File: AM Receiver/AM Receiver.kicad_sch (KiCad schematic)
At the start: 5 parts

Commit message: Finished PCB design for AM Receiver and fixed all remaining errors
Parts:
- H100: renamed from H1; now fitted
- H101: renamed from H3; now fitted
- H102: renamed from H2; now fitted
- H103: renamed from H4; now fitted
- PCB100: renamed from PCB1; now fitted
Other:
- note added: "Changes, Modifications V1.0 Initial Revision Input Voltage +/- 12V ... 15V"
- note added: "Date 01.07.2026"
- note added: "Name T.Brown"
- note added: "Rev. 1.0"
- note added: "Revision History"
- title: AM-Receiver -> AM Receiver

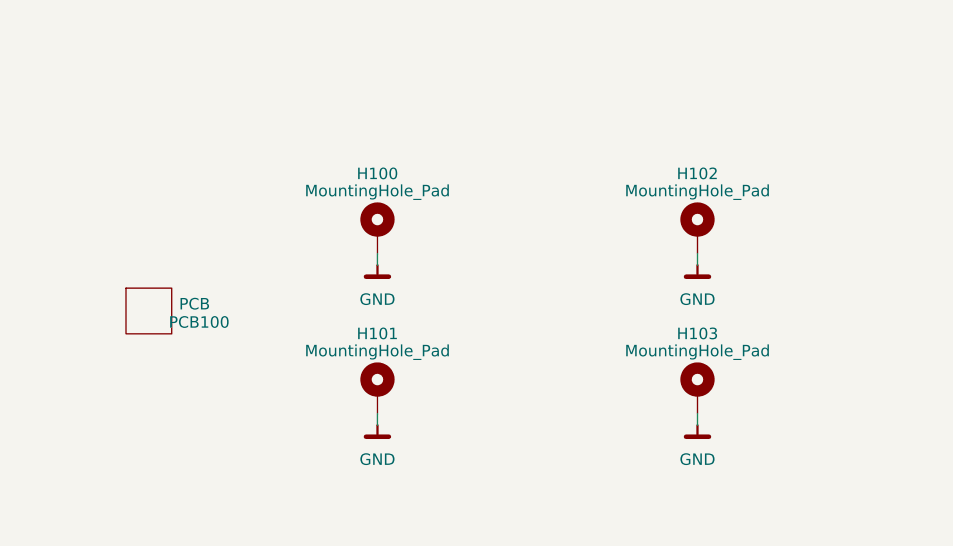
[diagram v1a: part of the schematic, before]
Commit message: Updated values of all resistors and capacitors
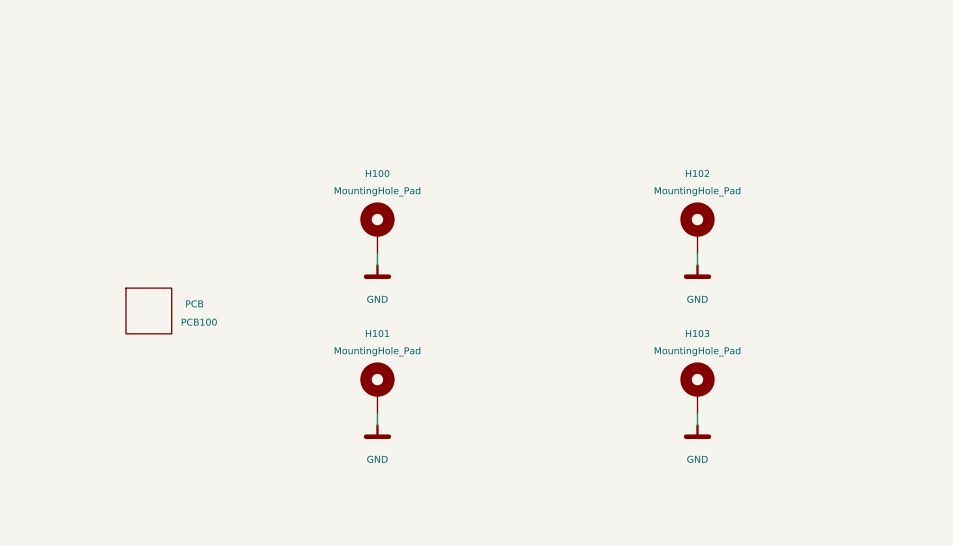
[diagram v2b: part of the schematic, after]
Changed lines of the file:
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@@
 			(effects
 				(font
-					(size 1.27 1.27)
+					(size 0.762 0.762)
 				)
 			)
@@
 			(effects
 				(font
-					(size 1.27 1.27)
+					(size 0.762 0.762)
 				)
 			)
@@
 			(effects
 				(font
-					(size 1.27 1.27)
+					(size 0.762 0.762)
 				)
 			)
@@
 			(effects
 				(font
-					(size 1.27 1.27)
+					(size 0.762 0.762)
 				)
 			)
@@
 			(effects
 				(font
-					(size 1.27 1.27)
+					(size 0.762 0.762)
 				)
 			)
@@
 			(effects
 				(font
-					(size 1.27 1.27)
+					(size 0.762 0.762)
 				)
 			)
@@
 			(effects
 				(font
-					(size 1.27 1.27)
+					(size 0.762 0.762)
 				)
 			)
@@
 			(effects
 				(font
-					(size 1.27 1.27)
+					(size 0.762 0.762)
 				)
 			)
@@
 			(effects
 				(font
-					(size 1.27 1.27)
+					(size 0.762 0.762)
 				)
 			)
@@
 			(effects
 				(font
-					(size 1.27 1.27)
+					(size 0.762 0.762)
 				)
 			)
@@
 			(effects
 				(font
-					(size 1.27 1.27)
+					(size 0.762 0.762)
 				)
 			)
@@
 			(effects
 				(font
-					(size 1.27 1.27)
+					(size 0.762 0.762)
 				)
 			)
@@
 			(effects
 				(font
-					(size 1.27 1.27)
+					(size 0.762 0.762)
 				)
 			)
@@
 			(effects
 				(font
-					(size 1.27 1.27)
+					(size 0.762 0.762)
 				)
 			)
@@
 			(effects
 				(font
-					(size 1.27 1.27)
+					(size 0.762 0.762)
 				)
 			)
@@
 			(effects
 				(font
-					(size 1.27 1.27)
+					(size 0.762 0.762)
 				)
 			)
@@
 			(effects
 				(font
-					(size 1.27 1.27)
+					(size 0.762 0.762)
 				)
 			)
@@
 			(effects
 				(font
-					(size 1.27 1.27)
-				)
-			)
+					(size 0.762 0.762)
+				)
+			)

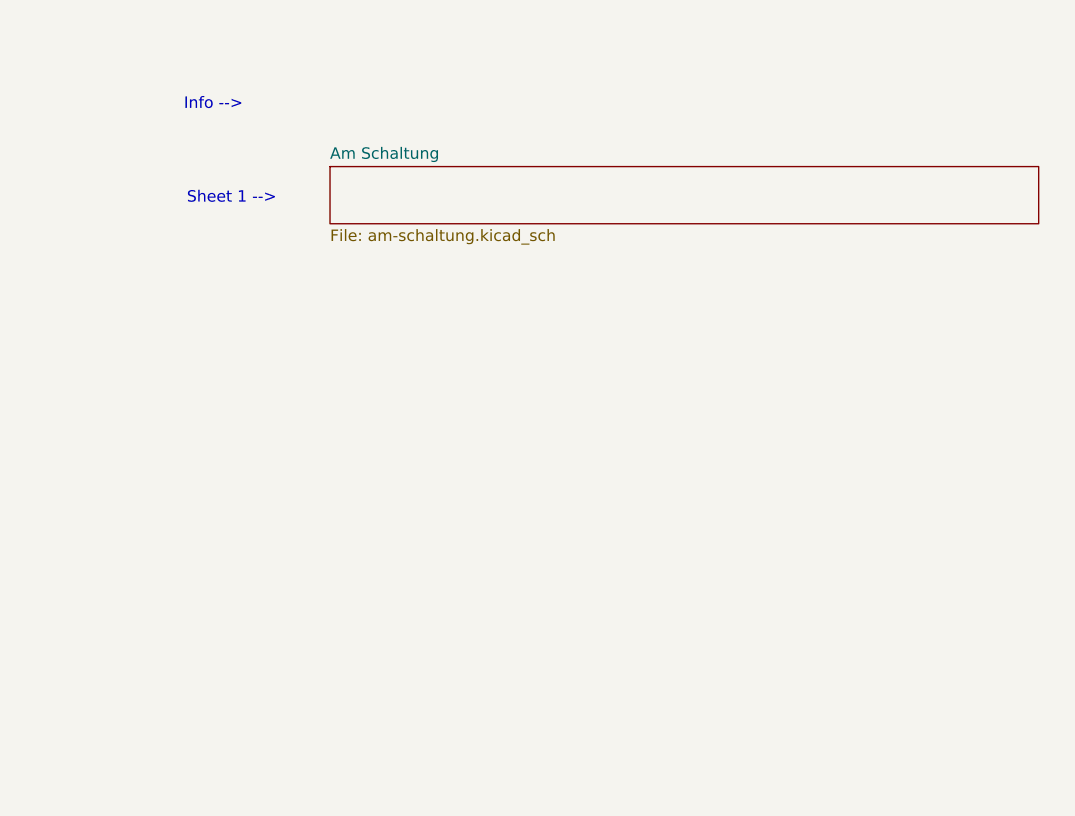
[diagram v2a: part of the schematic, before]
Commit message: Updated Schematic to use multiple sheets and repaired PCB
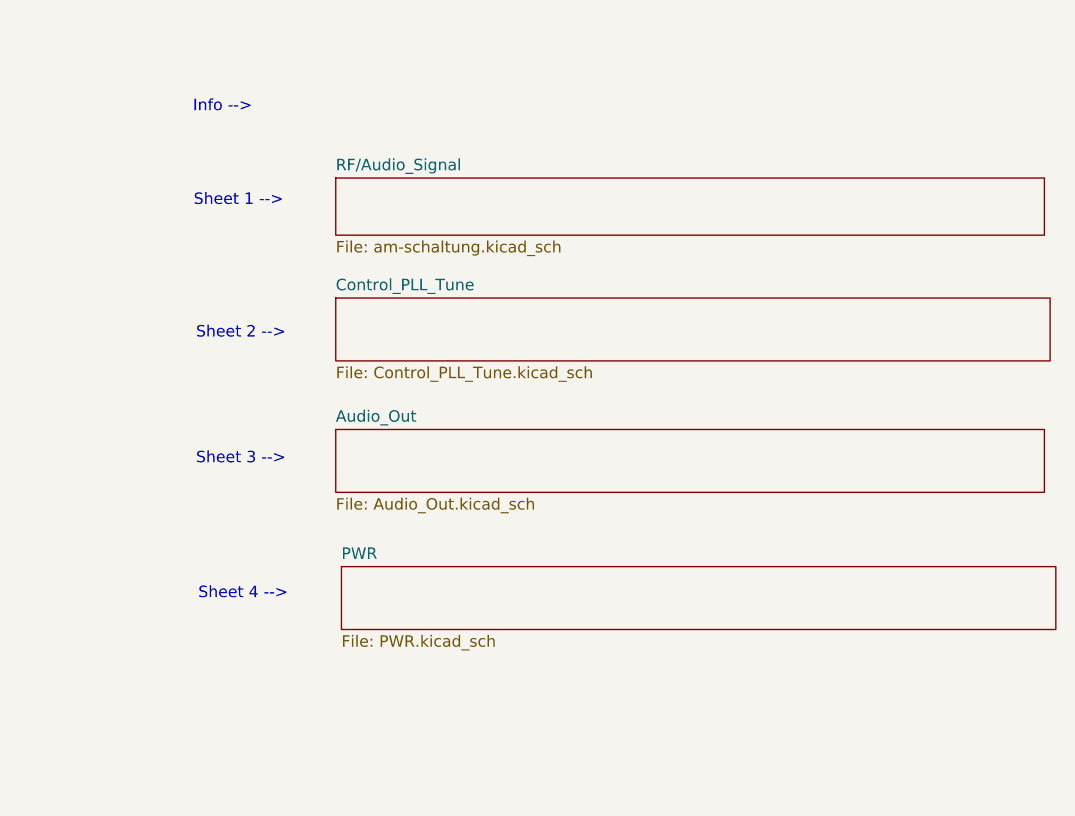
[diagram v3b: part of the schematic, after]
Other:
- sheet Am Schaltung renamed RF/Audio_Signal
- added sheet Audio_Out (Audio_Out.kicad_sch)
- added sheet Control_PLL_Tune (Control_PLL_Tune.kicad_sch)
- added sheet PWR (PWR.kicad_sch)
- note added: "Sheet 2 -->"
- note added: "Sheet 3 -->"
- note added: "Sheet 4 -->"
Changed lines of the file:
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@@
 	(title_block
 		(title "AM Receiver")
-		(date "2026-04-21")
+		(date "2026-07-06")
 		(rev "V1")
 		(company "HAWK")
@@
 	(text "Sheet 1 -->"
 		(exclude_from_sim no)
-		(at 189.738 35.306 0)
+		(at 190.5 35.56 0)
 		(effects
 			(font
@@
 	(text "Info -->"
 		(exclude_from_sim no)
-		(at 187.706 24.892 0)
+		(at 188.722 25.146 0)
+		(effects
+			(font
+				(size 1.27 1.27)
+			)
+		)
+	)
+	(text "Sheet 4 -->"
+		(exclude_from_sim no)
+		(at 191.008 79.248 0)
 		(effects
 			(font
@@
 		)
 	)
+	(text "Sheet 3 -->"
+		(exclude_from_sim no)
+		(at 190.754 64.262 0)
+		(effects
+			(font
+				(size 1.27 1.27)
+			)
+		)
+	)
 	(text "Name\nT.Brown"
 		(exclude_from_sim no)
@@
 			)
 			(justify left)
+		)
+	)
+	(text "Sheet 2 -->"
+		(exclude_from_sim no)
+		(at 190.754 50.292 0)
+		(effects
+			(font
+				(size 1.27 1.27)
+			)
 		)
 	)
@@
 	)
 	(sheet
-		(at 200.66 31.75)
-		(size 78.74 6.35)
+		(at 201.295 46.355)
+		(size 79.375 6.985)
 		(exclude_from_sim no)
 		(in_bom yes)
@@
 			(color 0 0 0 0)
 		)
-		(property "Sheetname" "Am Schaltung"
-			(at 200.66 31.0384 0)
+		(property "Sheetname" "Control_PLL_Tune"
+			(at 201.295 45.6434 0)
 			(show_name no)
 			(do_not_autoplace no)
@@
 			)
 		)
+		(property "Sheetfile" "Control_PLL_Tune.kicad_sch"
+			(at 201.295 53.9246 0)
+			(show_name no)
+			(do_not_autoplace no)
+			(effects
+				(font
+					(size 1.27 1.27)
+				)
+				(justify left top)
+			)
+		)
+		(instances
+			(project "AM Receiver"
+				(path "/fe1abb03-87b4-4c2c-a88f-7b58f4fb0195"
+					(page "3")
+				)
+			)
+		)
+	)
+	(sheet
+		(at 201.93 76.2)
+		(size 79.375 6.985)
+		(exclude_from_sim no)
+		(in_bom yes)
+		(on_board yes)
+		(dnp no)
+		(fields_autoplaced yes)
+		(stroke
+			(width 0.1524)
+			(type solid)
+		)
+		(fill
+			(color 0 0 0 0)
+		)
+		(property "Sheetname" "PWR"
+			(at 201.93 75.4884 0)
+			(show_name no)
+			(do_not_autoplace no)
+			(effects
+				(font
+					(size 1.27 1.27)
+				)
+				(justify left bottom)
+			)
+		)
+		(property "Sheetfile" "PWR.kicad_sch"
+			(at 201.93 83.7696 0)
+			(show_name no)
+			(do_not_autoplace no)
+			(effects
+				(font
+					(size 1.27 1.27)
+				)
+				(justify left top)
+			)
+		)
+		(instances
+			(project "AM Receiver"
+				(path "/fe1abb03-87b4-4c2c-a88f-7b58f4fb0195"
+					(page "5")
+				)
+			)
+		)
+	)
+	(sheet
+		(at 201.295 33.02)
+		(size 78.74 6.35)
+		(exclude_from_sim no)
+		(in_bom yes)
+		(on_board yes)
+		(dnp no)
+		(fields_autoplaced yes)
+		(stroke
+			(width 0.1524)
+			(type solid)
+		)
+		(fill
+			(color 0 0 0 0)
+		)
+		(property "Sheetname" "RF/Audio_Signal"
+			(at 201.295 32.3084 0)
+			(show_name no)
+			(do_not_autoplace no)
+			(effects
+				(font
+					(size 1.27 1.27)
+				)
+				(justify left bottom)
+			)
+		)
 		(property "Sheetfile" "am-schaltung.kicad_sch"
-			(at 200.66 38.6846 0)
+			(at 201.295 39.9546 0)
 			(show_name no)
 			(do_not_autoplace no)
@@
 				)
 			)
+		)
+	)
+	(sheet
+		(at 201.295 60.96)
+		(size 78.74 6.985)
+		(exclude_from_sim no)
+		(in_bom yes)
+		(on_board yes)
+		(dnp no)
+		(fields_autoplaced yes)
+		(stroke
+			(width 0.1524)
+			(type solid)
+		)
+		(fill
+			(color 0 0 0 0)
+		)
+		(property "Sheetname" "Audio_Out"
+			(at 201.295 60.2484 0)
+			(show_name no)
+			(do_not_autoplace no)
+			(effects
+				(font
+					(size 1.27 1.27)
+				)
+				(justify left bottom)
+			)
+		)
+		(property "Sheetfile" "Audio_Out.kicad_sch"
+			(at 201.295 68.5296 0)
+			(show_name no)
+			(do_not_autoplace no)
+			(effects
+				(font
+					(size 1.27 1.27)
+				)
+				(justify left top)
+			)
+		)
+		(instances
+			(project "AM Receiver"
+				(path "/fe1abb03-87b4-4c2c-a88f-7b58f4fb0195"
+					(page "4")
+				)
+			)

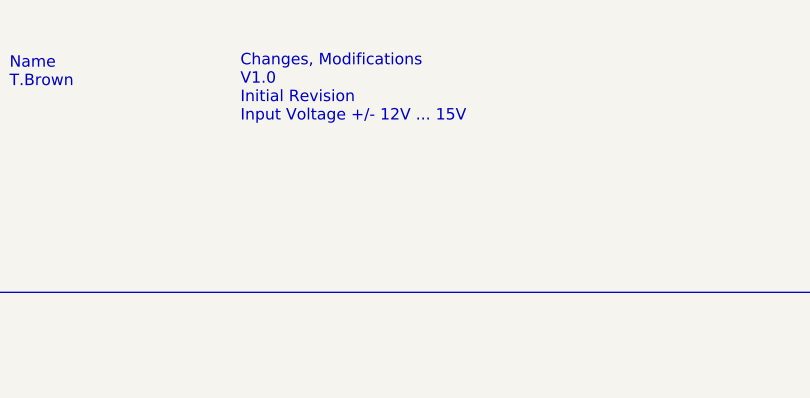
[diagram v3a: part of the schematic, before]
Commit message: updated schematic root page voltage
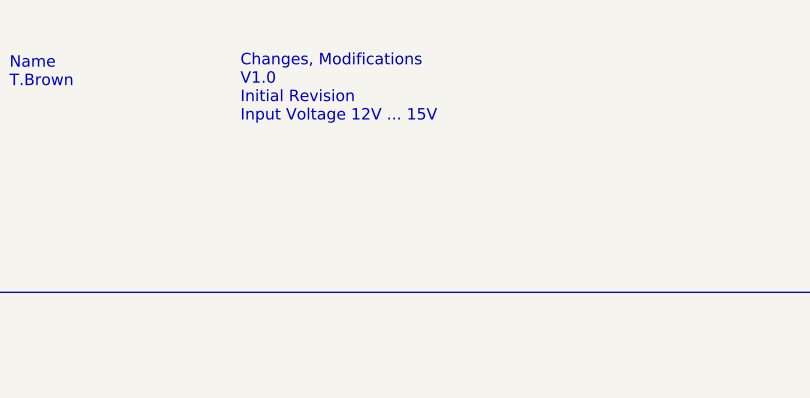
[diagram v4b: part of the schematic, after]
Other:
- note added: "Changes, Modifications V1.0 Initial Revision Input Voltage 12V ... 15V"
- note removed: "Changes, Modifications V1.0 Initial Revision Input Voltage +/- 12V ... 15V"
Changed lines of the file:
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@@
 		)
 	)
-	(text "Changes, Modifications\nV1.0\nInitial Revision\nInput Voltage +/- 12V ... 15V"
+	(text "Changes, Modifications\nV1.0\nInitial Revision\nInput Voltage 12V ... 15V"
 		(exclude_from_sim no)
 		(at 88.9 23.114 0)

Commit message: Updated Deckblatt
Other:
- note added: "Gruppe Gruppe 12"
- note added: "Projekt Am Receiver with quadratur mixer"
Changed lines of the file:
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@@
+		)
+	)
+	(text "Projekt\nAm Receiver with quadratur mixer"
+		(exclude_from_sim no)
+		(at 16.764 28.956 0)
+		(effects
+			(font
+				(size 1.27 1.27)
+			)
+			(justify left)
 		)
 	)
@@
 	(text "Name\nT.Brown"
 		(exclude_from_sim no)
-		(at 63.246 21.336 0)
+		(at 59.182 21.336 0)
 		(effects
 			(font
@@
 		(effects
 			(font
+				(size 1.27 1.27)
+			)
+			(justify left)
+		)
+	)
+	(text "Gruppe\nGruppe 12"
+		(exclude_from_sim no)
+		(at 75.184 21.59 0)
+		(effects
+			(font
